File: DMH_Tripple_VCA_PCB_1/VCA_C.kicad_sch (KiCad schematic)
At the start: 19 parts, among them Q5 BC548, Q6 BC548, U2 TL074

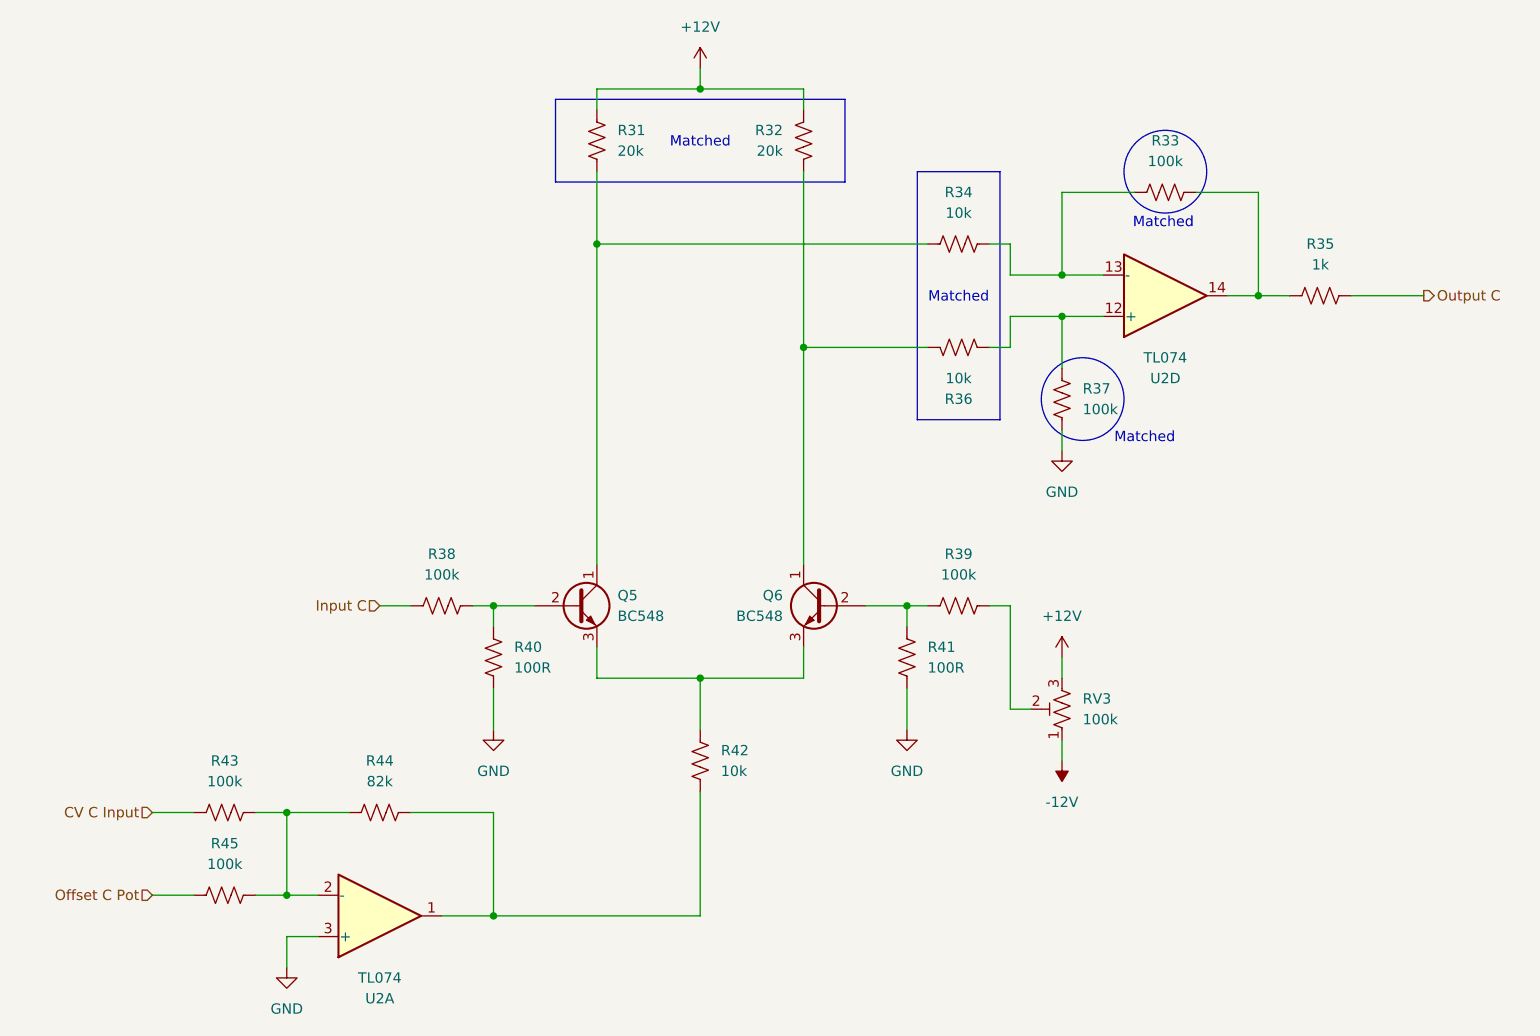
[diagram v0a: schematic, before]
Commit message: PCB 1 component positioning in progress
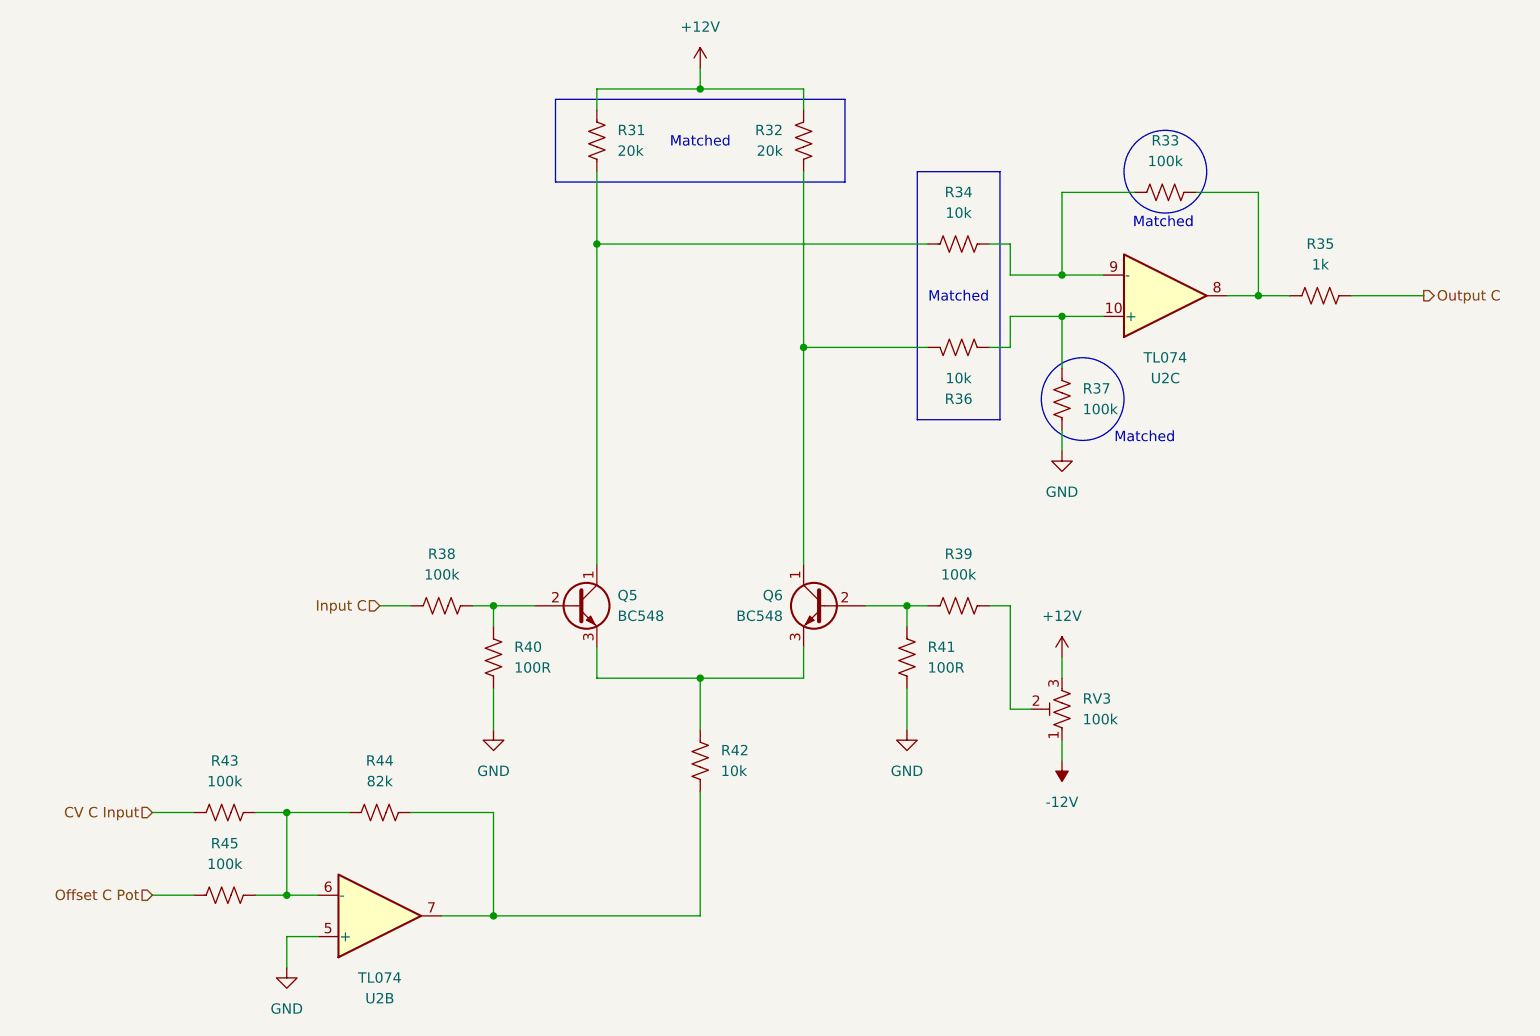
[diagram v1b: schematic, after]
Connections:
- net GND: now also U2.5 (+); no longer U2.3 (+)
- net at R33.1, R35.2: now also U2.8; no longer U2.14
- net at R33.2, R34.1: now also U2.9 (-); no longer U2.13 (-)
- net at R36.1, R37.1: now also U2.10 (+); no longer U2.12 (+)
- net at R42.1, R44.2: now also U2.7; no longer U2.1
- net at R43.2, R44.1, R45.2: now also U2.6 (-); no longer U2.2 (-)
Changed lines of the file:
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@@
 		(at 184.15 76.2 0)
 		(mirror x)
-		(unit 4)
+		(unit 3)
 		(exclude_from_sim no)
 		(in_bom yes)
@@
 				(path "/58f4306d-5387-4983-bb08-41a2313fd315/e5196600-83a1-4dc3-ad8c-62681c1f8ce4"
 					(reference "U2")
-					(unit 4)
+					(unit 3)
 				)
 			)
@@
 		(at 87.63 152.4 0)
 		(mirror x)
-		(unit 1)
+		(unit 2)
 		(exclude_from_sim no)
 		(in_bom yes)
@@
 				(path "/58f4306d-5387-4983-bb08-41a2313fd315/e5196600-83a1-4dc3-ad8c-62681c1f8ce4"
 					(reference "U2")
-					(unit 1)
+					(unit 2)
 				)
 			)

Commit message: Adjusted OpAmp pinouts for placement
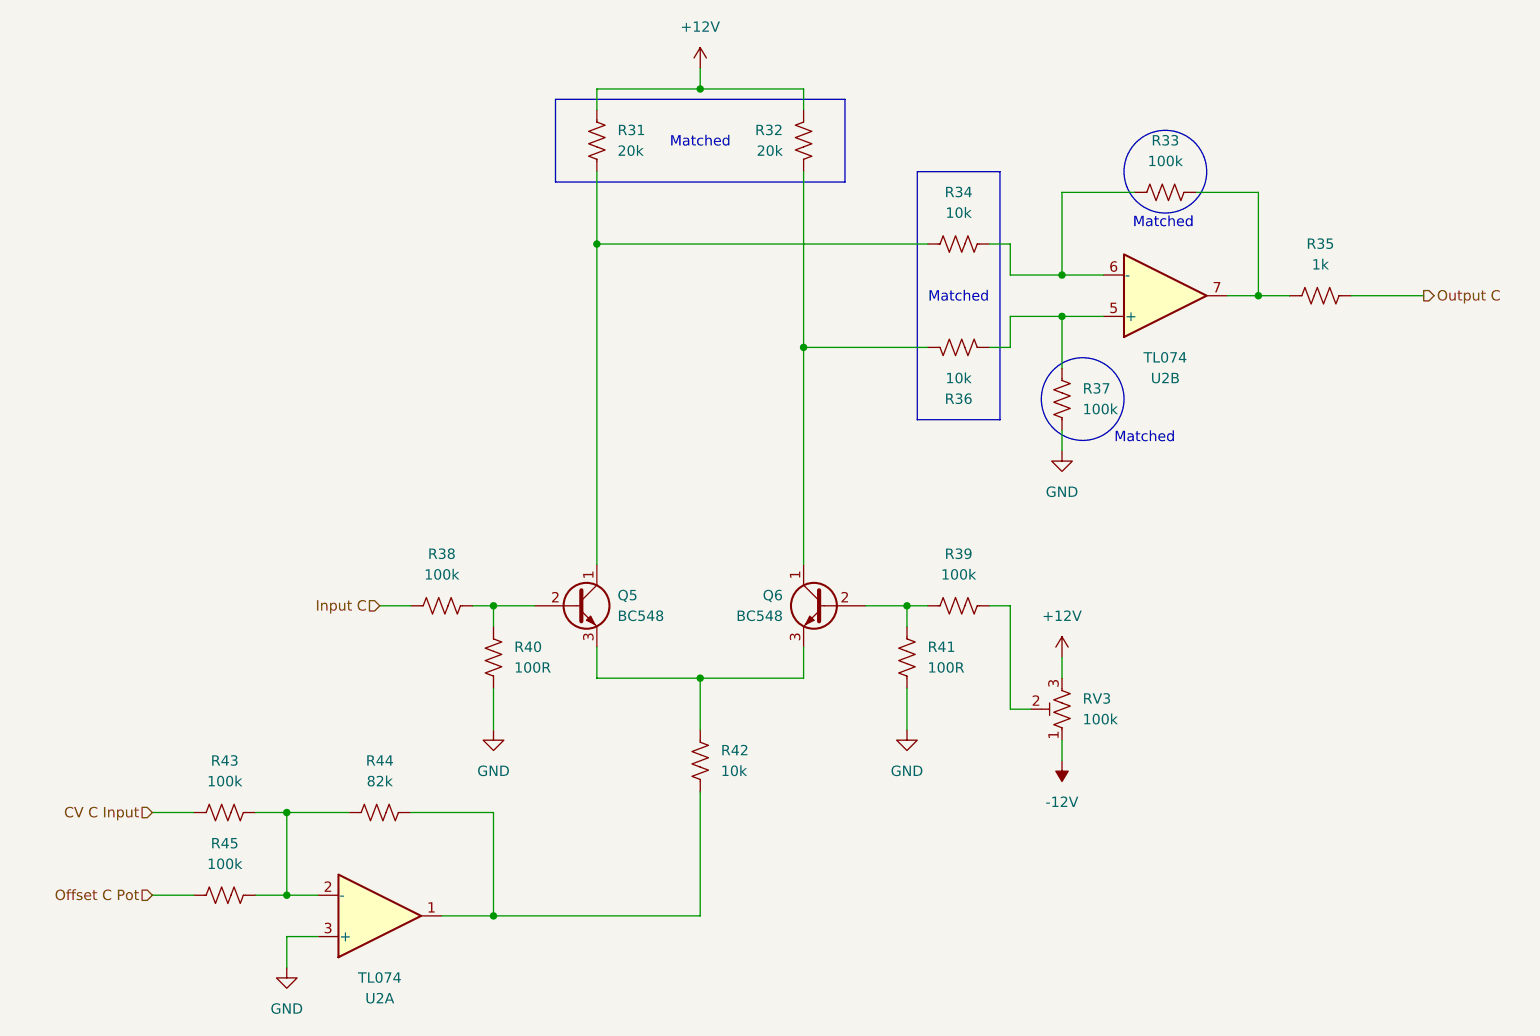
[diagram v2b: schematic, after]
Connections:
- net GND: now also U2.3 (+); no longer U2.5 (+)
- net at R33.1, R35.2: now also U2.7; no longer U2.8
- net at R33.2, R34.1: now also U2.6 (-); no longer U2.9 (-)
- net at R36.1, R37.1: now also U2.5 (+); no longer U2.10 (+)
- net at R43.2, R44.1, R45.2: now also U2.2 (-); no longer U2.6 (-)
- net at R42.1, R44.2: now also U2.1; no longer U2.7
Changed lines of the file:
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@@
 		(at 184.15 76.2 0)
 		(mirror x)
-		(unit 3)
+		(unit 2)
 		(exclude_from_sim no)
 		(in_bom yes)
@@
 				(path "/58f4306d-5387-4983-bb08-41a2313fd315/e5196600-83a1-4dc3-ad8c-62681c1f8ce4"
 					(reference "U2")
-					(unit 3)
+					(unit 2)
 				)
 			)
@@
 		(at 87.63 152.4 0)
 		(mirror x)
-		(unit 2)
+		(unit 1)
 		(exclude_from_sim no)
 		(in_bom yes)
@@
 				(path "/58f4306d-5387-4983-bb08-41a2313fd315/e5196600-83a1-4dc3-ad8c-62681c1f8ce4"
 					(reference "U2")
-					(unit 2)
+					(unit 1)
 				)
 			)

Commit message: Started routing over with upright resistor fps
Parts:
- R31, R32, R33, R34, R35, R36, R37, R38, R39, R40, R41, R42, R43, R44, R45: footprint Resistor_THT:R_Axial_DIN0207_L6.3mm_D2.5mm_P7.62mm_Horizontal -> Resistor_THT:R_Axial_DIN0207_L6.3mm_D2.5mm_P2.54mm_Vertical
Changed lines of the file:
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@@
 			)
 		)
-		(property "Footprint" "Resistor_THT:R_Axial_DIN0207_L6.3mm_D2.5mm_P7.62mm_Horizontal"
+		(property "Footprint" "Resistor_THT:R_Axial_DIN0207_L6.3mm_D2.5mm_P2.54mm_Vertical"
 			(at 183.896 64.516 90)
 			(effects
@@
 			)
 		)
-		(property "Footprint" "Resistor_THT:R_Axial_DIN0207_L6.3mm_D2.5mm_P7.62mm_Horizontal"
+		(property "Footprint" "Resistor_THT:R_Axial_DIN0207_L6.3mm_D2.5mm_P2.54mm_Vertical"
 			(at 151.384 120.396 90)
 			(effects
@@
 			)
 		)
-		(property "Footprint" "Resistor_THT:R_Axial_DIN0207_L6.3mm_D2.5mm_P7.62mm_Horizontal"
+		(property "Footprint" "Resistor_THT:R_Axial_DIN0207_L6.3mm_D2.5mm_P2.54mm_Vertical"
 			(at 202.946 77.216 90)
 			(effects
@@
 			)
 		)
-		(property "Footprint" "Resistor_THT:R_Axial_DIN0207_L6.3mm_D2.5mm_P7.62mm_Horizontal"
+		(property "Footprint" "Resistor_THT:R_Axial_DIN0207_L6.3mm_D2.5mm_P2.54mm_Vertical"
 			(at 100.584 120.396 90)
 			(effects
@@
 			)
 		)
-		(property "Footprint" "Resistor_THT:R_Axial_DIN0207_L6.3mm_D2.5mm_P7.62mm_Horizontal"
+		(property "Footprint" "Resistor_THT:R_Axial_DIN0207_L6.3mm_D2.5mm_P2.54mm_Vertical"
 			(at 158.496 81.534 90)
 			(effects
@@
 			)
 		)
-		(property "Footprint" "Resistor_THT:R_Axial_DIN0207_L6.3mm_D2.5mm_P7.62mm_Horizontal"
+		(property "Footprint" "Resistor_THT:R_Axial_DIN0207_L6.3mm_D2.5mm_P2.54mm_Vertical"
 			(at 94.996 115.316 90)
 			(effects
@@
 			)
 		)
-		(property "Footprint" "Resistor_THT:R_Axial_DIN0207_L6.3mm_D2.5mm_P7.62mm_Horizontal"
+		(property "Footprint" "Resistor_THT:R_Axial_DIN0207_L6.3mm_D2.5mm_P2.54mm_Vertical"
 			(at 113.284 56.896 90)
 			(effects
@@
 			)
 		)
-		(property "Footprint" "Resistor_THT:R_Axial_DIN0207_L6.3mm_D2.5mm_P7.62mm_Horizontal"
+		(property "Footprint" "Resistor_THT:R_Axial_DIN0207_L6.3mm_D2.5mm_P2.54mm_Vertical"
 			(at 158.496 115.316 90)
 			(effects
@@
 			)
 		)
-		(property "Footprint" "Resistor_THT:R_Axial_DIN0207_L6.3mm_D2.5mm_P7.62mm_Horizontal"
+		(property "Footprint" "Resistor_THT:R_Axial_DIN0207_L6.3mm_D2.5mm_P2.54mm_Vertical"
 			(at 158.496 70.866 90)
 			(effects
@@
 			)
 		)
-		(property "Footprint" "Resistor_THT:R_Axial_DIN0207_L6.3mm_D2.5mm_P7.62mm_Horizontal"
+		(property "Footprint" "Resistor_THT:R_Axial_DIN0207_L6.3mm_D2.5mm_P2.54mm_Vertical"
 			(at 87.884 138.684 90)
 			(effects
@@
 			)
 		)
-		(property "Footprint" "Resistor_THT:R_Axial_DIN0207_L6.3mm_D2.5mm_P7.62mm_Horizontal"
+		(property "Footprint" "Resistor_THT:R_Axial_DIN0207_L6.3mm_D2.5mm_P2.54mm_Vertical"
 			(at 172.466 89.154 90)
 			(effects
@@
 			)
 		)
-		(property "Footprint" "Resistor_THT:R_Axial_DIN0207_L6.3mm_D2.5mm_P7.62mm_Horizontal"
+		(property "Footprint" "Resistor_THT:R_Axial_DIN0207_L6.3mm_D2.5mm_P2.54mm_Vertical"
 			(at 68.834 138.684 90)
 			(effects
@@
 			)
 		)
-		(property "Footprint" "Resistor_THT:R_Axial_DIN0207_L6.3mm_D2.5mm_P7.62mm_Horizontal"
+		(property "Footprint" "Resistor_THT:R_Axial_DIN0207_L6.3mm_D2.5mm_P2.54mm_Vertical"
 			(at 68.834 148.844 90)
 			(effects
@@
 			)
 		)
-		(property "Footprint" "Resistor_THT:R_Axial_DIN0207_L6.3mm_D2.5mm_P7.62mm_Horizontal"
+		(property "Footprint" "Resistor_THT:R_Axial_DIN0207_L6.3mm_D2.5mm_P2.54mm_Vertical"
 			(at 140.716 56.896 90)
 			(effects
@@
 			)
 		)
-		(property "Footprint" "Resistor_THT:R_Axial_DIN0207_L6.3mm_D2.5mm_P7.62mm_Horizontal"
+		(property "Footprint" "Resistor_THT:R_Axial_DIN0207_L6.3mm_D2.5mm_P2.54mm_Vertical"
 			(at 125.984 133.096 90)
 			(effects

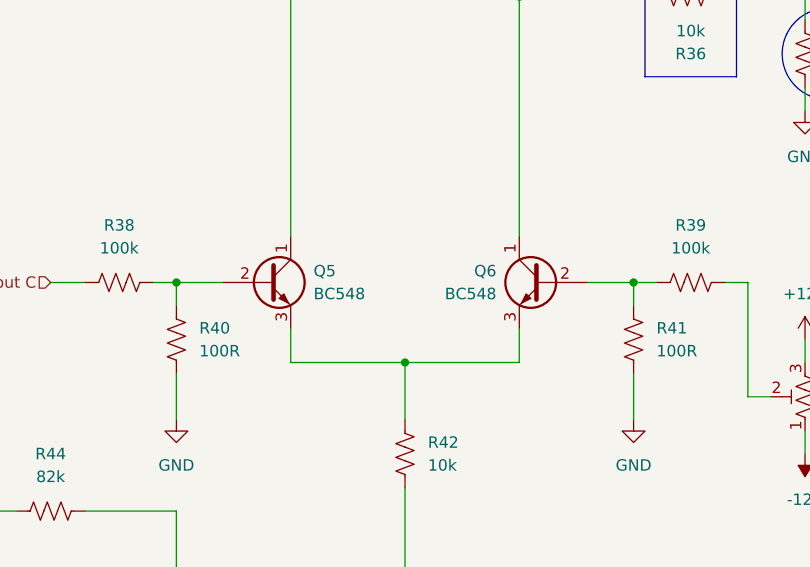
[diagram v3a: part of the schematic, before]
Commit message: Converted PCB 1 project to KiCad 9
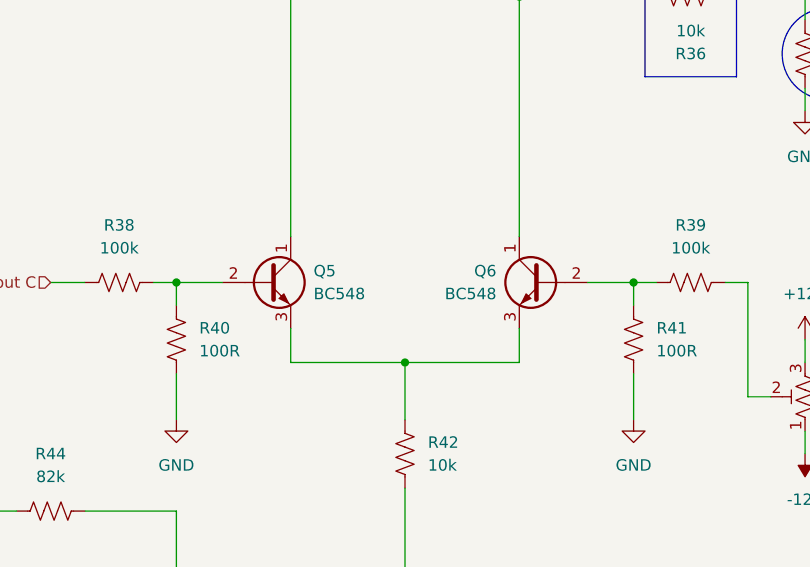
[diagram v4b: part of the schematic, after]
